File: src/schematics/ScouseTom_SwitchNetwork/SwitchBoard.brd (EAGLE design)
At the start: 169.5 x 97.5 mm, 87 parts, among them T1 PNP, U1 MCP73831, U10 ADG714BRUZ, U11 ADG714BRUZ, U12 ADUM1410ARWZ, U13 ADG714BRUZ, U14 ADG714BRUZ, U15 ADUM1412ARWZ, U2 ADG714BRUZ, U3 ADG714BRUZ, U4 TPS61090RSAR, U5 ADG714BRUZ, U6 ADG714BRUZ, U7 ADG714BRUZ, U8 LT1763CDE-5, U9 ADG714BRUZ, X1 USB-MICROB, X2 CTR_ARD, X3 CTR_OUT, X4 DSUB _T, X5 DSUB_B, X6 CTR_IN

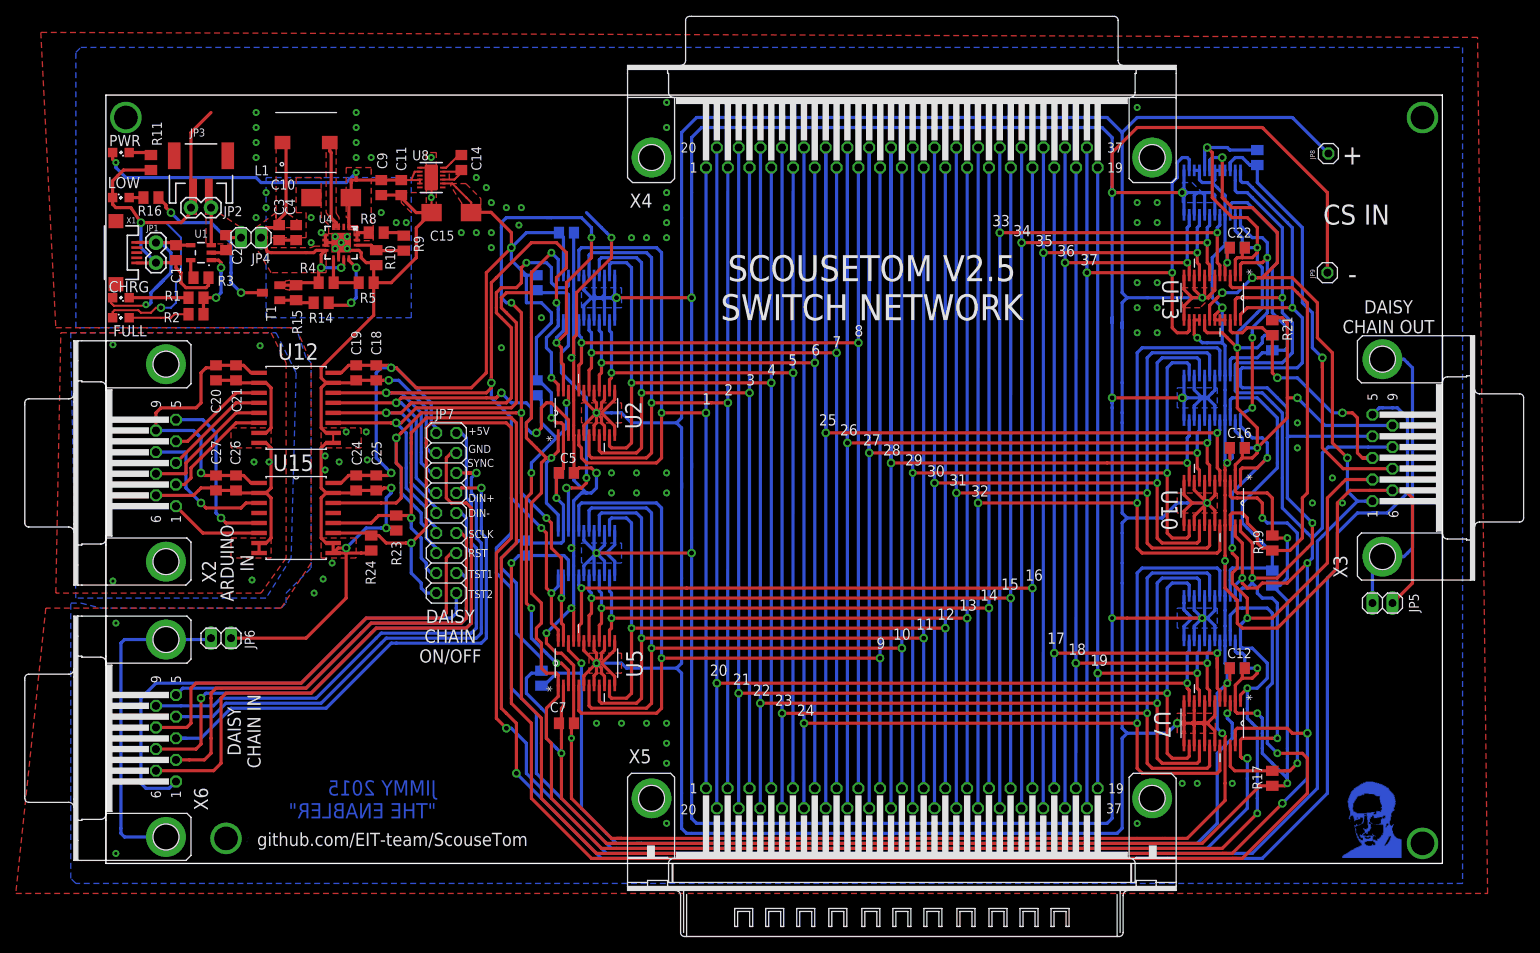
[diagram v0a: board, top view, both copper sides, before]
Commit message: updated switchboard with proper daisy chain select and test 1 correct wiring
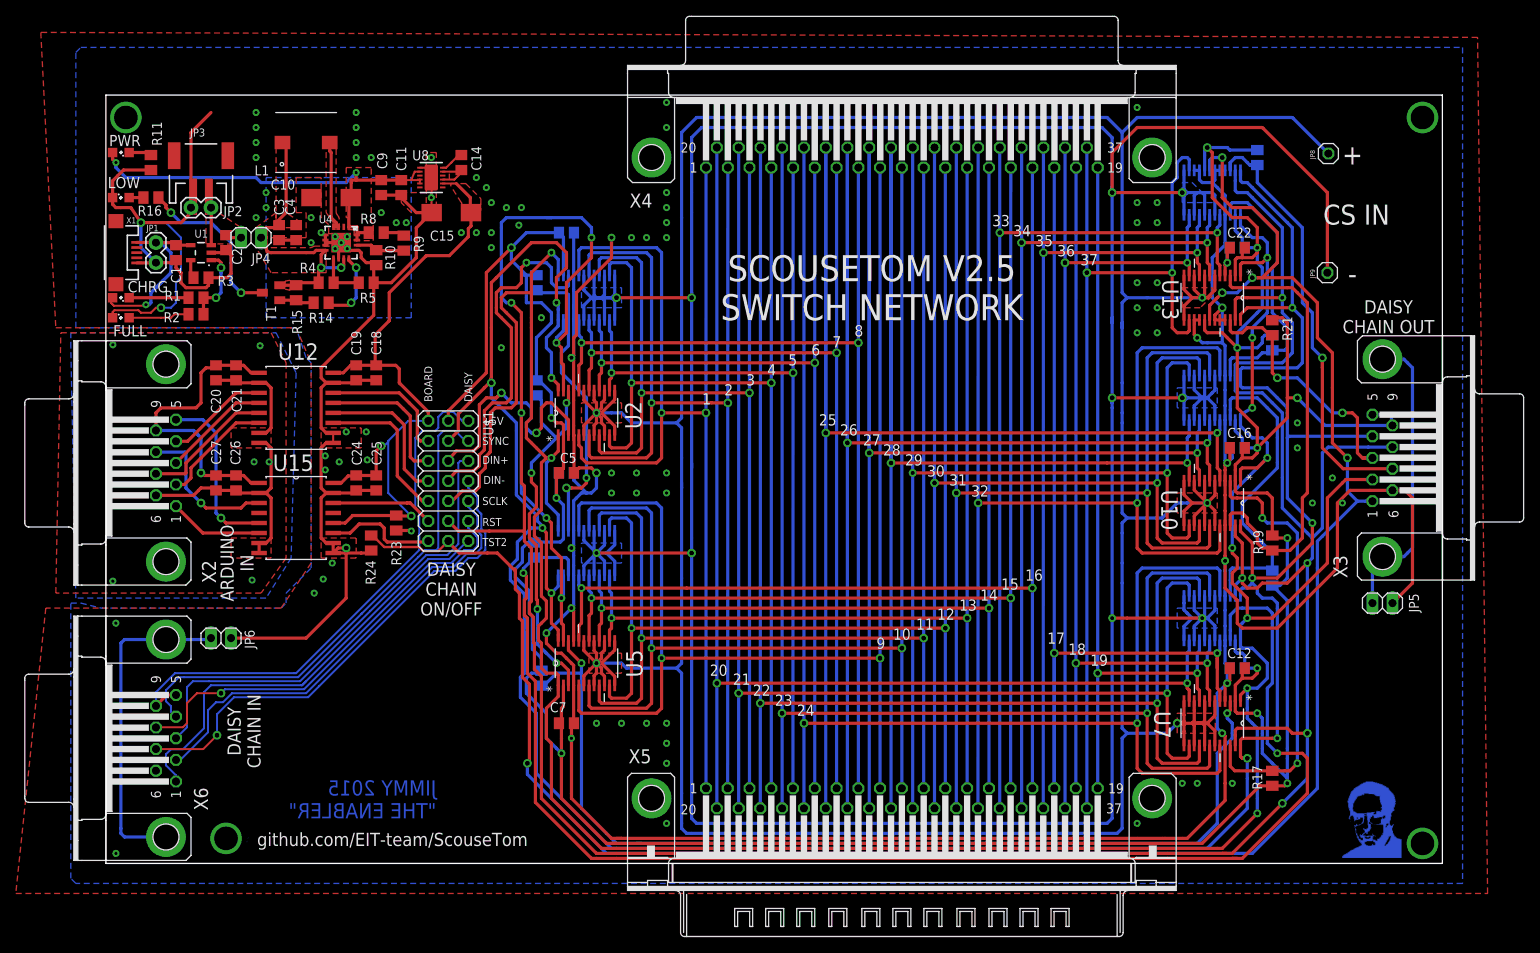
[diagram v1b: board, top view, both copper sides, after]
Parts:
- removed JP7: DCHN, pinhead:2X09
- added U$1: PINHD-3X7GAP, pinhead:3X07
- moved R13 1.05 mm to (37.2, 44.2)
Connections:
- removed net GND_DCHN: JP7.4, X6.6
- removed net RESET_DCHN: JP7.14, X6.8
- removed net SYNC_DCHN: JP7.6, X6.4
- removed net TEST_1: JP7.15, R23.2, U15.12, X3.5
- removed net TEST_1_DCHN: JP7.16, X6.5
- new net DIN+_BRD: U$1.5, U12.13
- new net DIN-_BRD: U$1.7, U12.12
- new net SCLK_BRD: U$1.9, U12.11
- new net TEST_2_BRD: U$1.13, U15.11
- new net VDD_BRD: C15.+, C18.1, C19.1, C24.1, C25.1, R23.2, U$1.1, U12.16, U15.12, U15.16, U8.2
- new net ~RESET_BRD: U$1.11, U15.14
- new net ~RESET_DCHN: U$1.12, X6.8
- new net ~SYNC_BRD: U$1.3, U12.14
- new net ~SYNC_DCHN: U$1.4, X6.4
- net AGND: now also X6.6; no longer JP7.3
- net DIN+: now also U$1.17; no longer JP7.7, U12.13
- net DIN+_DCHN: now also U$1.6; no longer JP7.8
- net DIN-: now also U$1.18; no longer JP7.9, U12.12
- net DIN-_DCHN: now also U$1.8; no longer JP7.10
- net SCLK: now also U$1.19; no longer JP7.11, U12.11
- net SCLK_DCHN: now also U$1.10; no longer JP7.12
- net TEST_2: now also U$1.21; no longer JP7.17, U15.11
- net TEST_2_DCHN: now also U$1.14; no longer JP7.18
- net VDD: now also U$1.15, X3.5; no longer C15.+, C18.1, C19.1, C24.1, C25.1, JP7.1, U12.16, U15.16, U8.2
- net VDD_DCHN: now also U$1.2, X6.5; no longer JP7.2
- net ~RESET: now also U$1.20; no longer JP7.13, U15.14
- net ~SYNC: now also U$1.16; no longer JP7.5, U12.14
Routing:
- net TEST_1: track 261.1 -> 0.00 mm, vias 2 -> 0
- net VDD_BRD: track 0.00 -> 87.6 mm, vias 0 -> 2
- net GND_DCHN: track 77.5 -> 0.00 mm
- net SYNC_DCHN: track 68.0 -> 0.00 mm, vias 1 -> 0
- net ~SYNC_DCHN: track 0.00 -> 64.8 mm
- net VDD: track 506.0 -> 441.4 mm, vias 15 -> 13
- net ~RESET_DCHN: track 0.00 -> 55.6 mm, vias 0 -> 1
- net RESET_DCHN: track 54.0 -> 0.00 mm
- net TEST_1_DCHN: track 47.5 -> 0.00 mm
- net TEST_2: track 311.2 -> 266.5 mm, vias 6 -> 5
- net ~RESET: track 458.1 -> 417.8 mm, vias 12 -> 11
- net ~SYNC: track 392.0 -> 364.6 mm, vias 11 -> 10
- net AGND: track 612.2 -> 585.8 mm, vias 109 -> 107
- net DIN-: track 70.1 -> 46.0 mm, vias 2 -> 1
- net SCLK: track 376.8 -> 354.3 mm, vias 11 -> 10
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- added copper zone on layer 1, net VDD_BRD
- removed copper zone on layer 1, net VDD
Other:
- board text added: "BOARD"
- board text added: "DAISY"
- board text added: "SELECT"

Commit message: minor changes to board before sending to PCBTrain
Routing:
- net VDD_BRD: track 87.6 -> 85.9 mm
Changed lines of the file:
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@@
 <wire x1="22.225" y1="81.28" x2="19.05" y2="78.105" width="0.4064" layer="1"/>
 <wire x1="19.05" y1="78.105" x2="16.825" y2="78.105" width="0.4064" layer="1"/>
-<wire x1="10.16" y1="67.31" x2="16.825" y2="73.975" width="0.4064" layer="1"/>
-<wire x1="16.825" y1="73.975" x2="16.825" y2="78.105" width="0.4064" layer="1"/>
 <via x="29.845" y="91.44" extent="1-16" drill="0.4"/>
-<via x="31.115" y="90.17" extent="1-16" drill="0.4"/>
+<via x="31.75" y="90.297" extent="1-16" drill="0.4"/>
 <via x="31.75" y="88.265" extent="1-16" drill="0.4"/>
-<via x="31.75" y="84.455" extent="1-16" drill="0.4"/>
+<via x="31.75" y="84.201" extent="1-16" drill="0.4"/>
 <via x="31.75" y="82.55" extent="1-16" drill="0.4"/>
 <via x="10.16" y="84.455" extent="1-16" drill="0.4"/>
@@
 <via x="33.02" y="69.85" extent="1-16" drill="0.4"/>
 <via x="38.1" y="73.66" extent="1-16" drill="0.4"/>
-<via x="35.2425" y="85.4075" extent="1-16" drill="0.4"/>
+<via x="35.4965" y="85.4075" extent="1-16" drill="0.4"/>
 <via x="33.655" y="87.63" extent="1-16" drill="0.4"/>
-<via x="35.56" y="87.63" extent="1-16" drill="0.4"/>
+<via x="35.433" y="87.63" extent="1-16" drill="0.4"/>
 <via x="53.975" y="22.225" extent="1-16" drill="0.4"/>
 <via x="53.975" y="17.145" extent="1-16" drill="0.4"/>
 <via x="53.975" y="9.525" extent="1-16" drill="0.4"/>
 <via x="41.91" y="20.32" extent="1-16" drill="0.4"/>
-<via x="29.845" y="84.455" extent="1-16" drill="0.4"/>
-<via x="27.94" y="84.455" extent="1-16" drill="0.4"/>
+<via x="29.591" y="84.201" extent="1-16" drill="0.4"/>
+<via x="26.67" y="84.201" extent="1-16" drill="0.4"/>
 <via x="16.51" y="93.98" extent="1-16" drill="0.4"/>
 <via x="14.605" y="93.98" extent="1-16" drill="0.4"/>
@@
 <wire x1="-1.27" y1="79.248" x2="-1.27" y2="81.6" width="0.4064" layer="1"/>
 <wire x1="-1.27" y1="81.6" x2="-1.905" y2="82.235" width="0.4064" layer="1"/>
+<wire x1="10.16" y1="67.31" x2="10.16" y2="70.231" width="0.4064" layer="1"/>
+<wire x1="10.16" y1="70.231" x2="15.494" y2="75.565" width="0.4064" layer="1"/>
+<wire x1="16.825" y1="78.105" x2="16.825" y2="76.896" width="0.4064" layer="1"/>
+<wire x1="16.825" y1="76.896" x2="15.494" y2="75.565" width="0.4064" layer="1"/>
 </signal>
 <signal name="SCLK">
@@
 <wire x1="14.60459375" y1="67.624796875" x2="17.144796875" y2="67.624796875" width="0.4064" layer="1"/>
 <wire x1="29.17" y1="86.995" x2="29.17" y2="85.304" width="0.4064" layer="1"/>
-<wire x1="29.17" y1="85.304" x2="28.829" y2="84.963" width="0.4064" layer="1"/>
-<wire x1="28.829" y1="84.963" x2="28.829" y2="83.947" width="0.4064" layer="1"/>
-<wire x1="28.829" y1="83.947" x2="26.416" y2="81.534" width="0.4064" layer="1"/>
-<wire x1="26.416" y1="81.534" x2="23.495" y2="81.534" width="0.4064" layer="1"/>
-<wire x1="23.495" y1="81.534" x2="18.796" y2="76.835" width="0.4064" layer="1"/>
-<wire x1="18.796" y1="76.835" x2="18.796" y2="73.279" width="0.4064" layer="1"/>
-<wire x1="18.796" y1="73.279" x2="17.018" y2="71.501" width="0.4064" layer="1"/>
 <wire x1="17.018" y1="71.501" x2="17.018" y2="67.75159375" width="0.4064" layer="1"/>
 <wire x1="17.018" y1="67.75159375" x2="17.144796875" y2="67.624796875" width="0.4064" layer="1"/>
@@
 <wire x1="17.78" y1="57.404" x2="18.161" y2="57.404" width="0.4064" layer="16"/>
 <wire x1="18.161" y1="57.404" x2="18.669" y2="57.912" width="0.254" layer="16"/>
+<wire x1="17.018" y1="71.501" x2="17.018" y2="73.152" width="0.4064" layer="1"/>
+<wire x1="17.018" y1="73.152" x2="29.17" y2="85.304" width="0.4064" layer="1"/>
 </signal>
 <signal name="~SYNC_BRD">
